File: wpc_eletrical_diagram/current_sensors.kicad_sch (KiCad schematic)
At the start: 4 parts

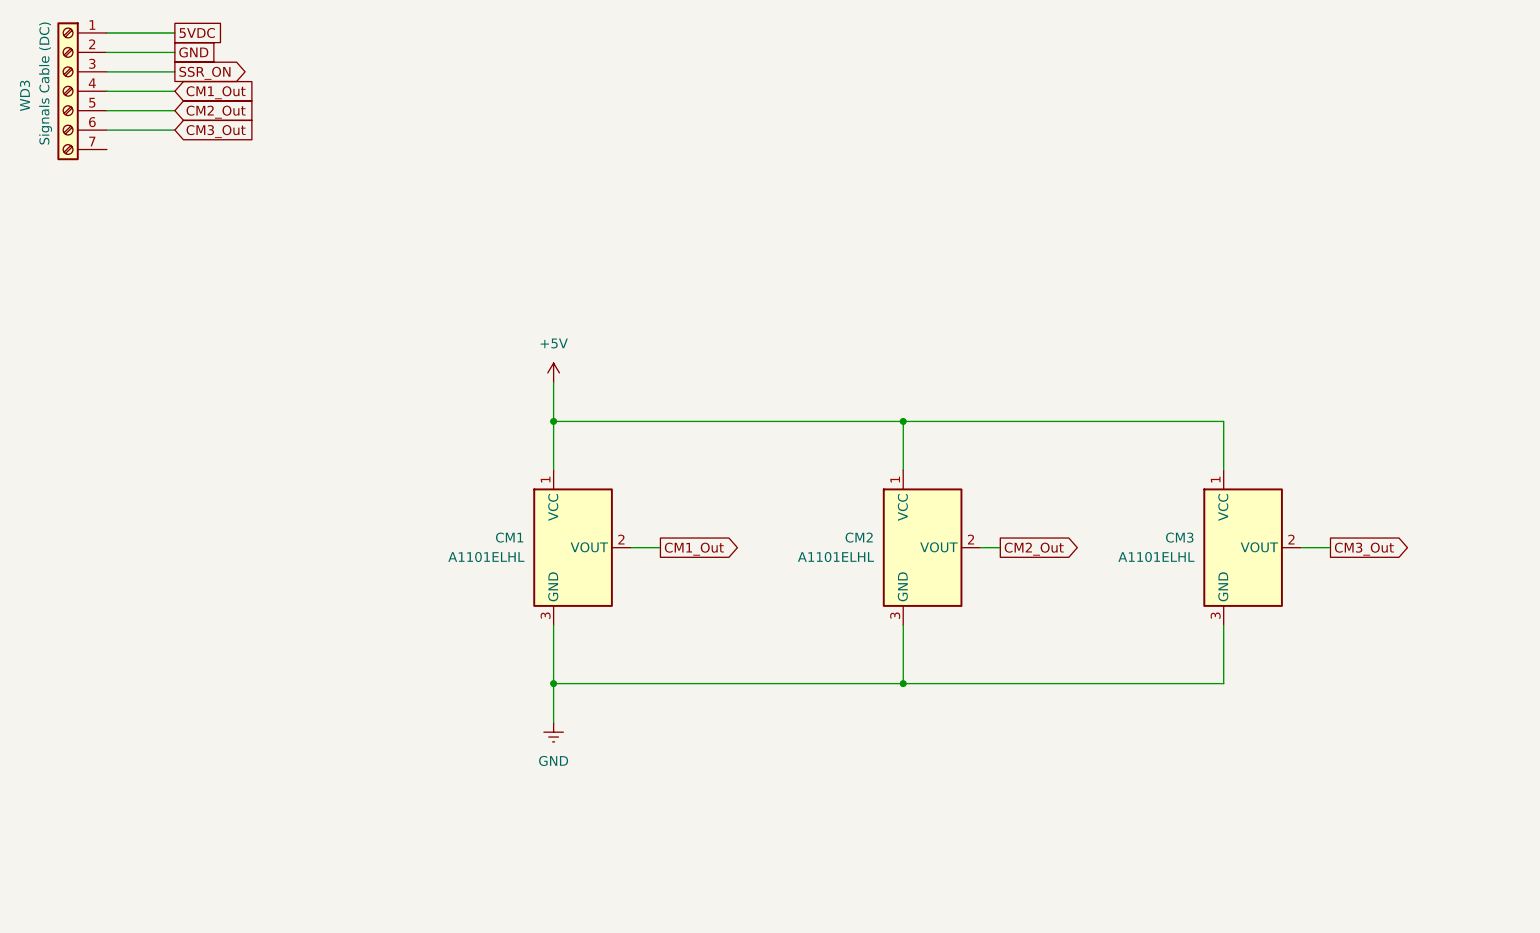
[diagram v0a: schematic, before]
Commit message: eletrical corrections
- schematic correction (sensors, actuation)
- main board correction (resistor values, chottky diodes) (v26)
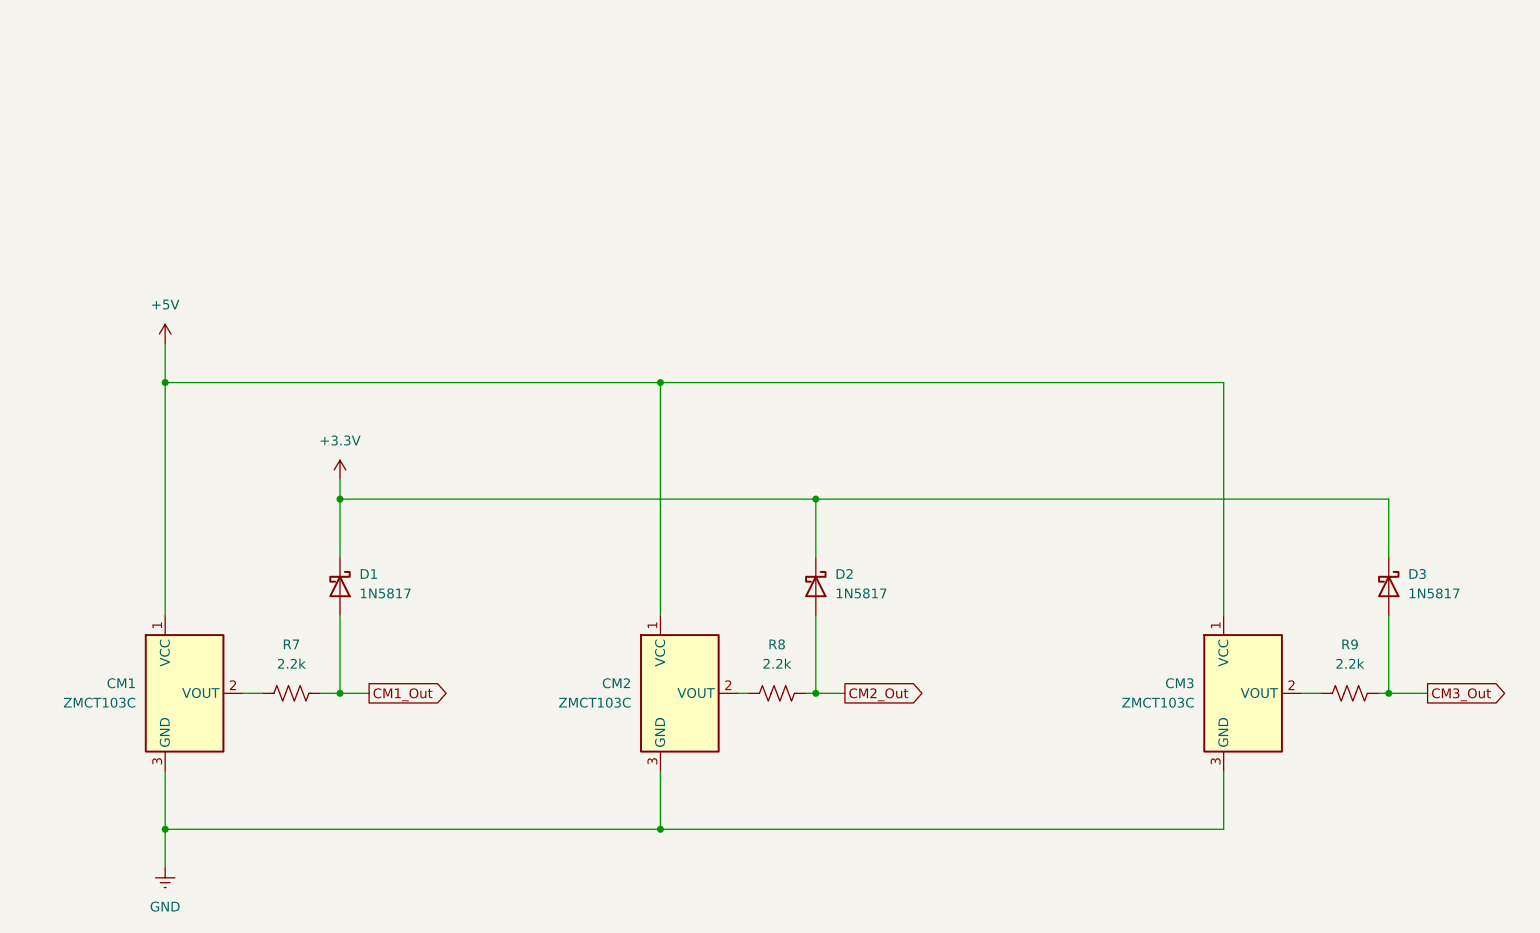
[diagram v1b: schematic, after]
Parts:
- removed WD3: Signals Cable (DC), symbol Connector:Screw_Terminal_01x07
- added D1, D2, D3: 1N5817, symbol Device:D_Schottky
- added R7, R8, R9: 2.2k, symbol Device:R_US
- CM1, CM2, CM3: value A1101ELHL -> ZMCT103C
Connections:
- net CM1_Out: now also D1.2 (A), R7.2; no longer CM1.2 (VOUT)
- net CM2_Out: now also D2.2 (A), R8.2; no longer CM2.2 (VOUT)
- net CM3_Out: now also D3.2 (A), R9.2; no longer CM3.2 (VOUT)
- new net: CM3.2 (VOUT), R9.1
- new net: CM1.2 (VOUT), R7.1
- new net: CM2.2 (VOUT), R8.1
- new net +3.3V: D1.1 (K), D2.1 (K), D3.1 (K)
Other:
- moved on the sheet: CM1, CM2, CM3
